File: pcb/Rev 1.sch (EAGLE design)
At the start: 50 parts, among them J1 3220-10-0100-00, U1 ATSAMD21G18A-MU, U2 AP3441, U3 TPS61089

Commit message: Worked on the schematic some more
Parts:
- added C26, C27, C28, C29, C30, C31, C32, C33, C42, C43, C44, C45, C46, C47, C48, C49, C50, C51, C58, C59: 1uF, Micromouse 2020:CAPACITOR0805
- added C34, C35, C36, C37, C38, C39, C40, C41, C52, C55: 0.1uF, Micromouse 2020:CAPACITOR0805
- added C53: 0.12uF, Micromouse 2020:CAPACITOR0805
- added C54: 6800pF, Micromouse 2020:CAPACITOR0805
- added C56, C57: 22pF, Micromouse 2020:CAPACITOR0805
- added D1, D10, D11, D2, D3, D4, D5, D6, D7, D8, D9: LED, Micromouse 2020:LED
- added D12, D13, D14, D15, D16, D17, D18, D19: SFH4545, Micromouse 2020:SFH4545
- added Q1, Q10, Q11, Q12, Q13, Q14, Q15, Q2, Q20, Q21, Q22, Q23, Q3, Q4, Q5, Q6, Q7, Q8, Q9: MMBT3904,215MMBT3904,215, Micromouse 2020:MMBT3904,215MMBT3904,215
- added Q16, Q17, Q18, Q19, Q24, Q25, Q26, Q27: TEFT4300, Micromouse 2020:TEFT4300
- added R15, R16, R17, R18, R19, R20, R21, R22, R23, R24, R25: (no value), Micromouse 2020:RESISTOR0805
- added R26, R27, R28, R29, R34, R35, R36, R37: 20R, Micromouse 2020:RESISTOR0805
- added R30, R31, R32, R33, R38, R39, R40, R41: 1k, Micromouse 2020:RESISTOR0805
- added R42, R43, R44, R45, R46, R47, R48, R49: 10k, Micromouse 2020:RESISTOR0805
- added R50, R51: 4.7k, Micromouse 2020:RESISTOR0805
- added U4: BNO055, Micromouse 2020:BNO055
- added U5: MCP73811, Micromouse 2020:MCP73811
- added XTAL3: 32.768kHz, Micromouse 2020:FC-135
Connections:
- new net IMU_INT: U4.INT
- new net IR1: Q12.B
- new net IR2: Q13.B
- new net IR3: Q14.B
- new net IR4: Q15.B
- new net IR5: Q20.B
- new net IR6: Q21.B
- new net IR7: Q22.B
- new net IR8: Q23.B
- new net LED0: Q2.B
- new net LED1: Q3.B
- new net LED2: Q4.B
- new net LED3: Q5.B
- new net LED4: Q6.B
- new net LED5: Q7.B
- new net LED6: Q8.B
- new net LED7: Q9.B
- new net LED8: Q10.B
- new net LED9: Q11.B
- new net N$16: Q1.B, U2.PG
- new net N$18: D1.OUT, Q1.C
- new net N$19: D1.IN, R15.P$1
- new net N$20: D2.OUT, Q2.C
- new net N$21: D2.IN, R16.P$1
- new net N$22: D3.OUT, Q3.C
- new net N$23: D3.IN, R17.P$1
- new net N$24: D4.OUT, Q4.C
- new net N$25: D4.IN, R18.P$1
- new net N$26: D5.OUT, Q5.C
- new net N$27: D5.IN, R19.P$1
- new net N$28: D6.OUT, Q6.C
- new net N$29: D6.IN, R20.P$1
- new net N$30: D7.OUT, Q7.C
- new net N$31: D7.IN, R21.P$1
- new net N$32: D8.OUT, Q8.C
- new net N$33: D8.IN, R22.P$1
- new net N$34: D9.OUT, Q9.C
- new net N$35: D9.IN, R23.P$1
- new net N$36: D10.OUT, Q10.C
- new net N$37: D10.IN, R24.P$1
- new net N$38: D11.OUT, Q11.C
- new net N$39: D11.IN, R25.P$1
- new net N$40: D12.OUT, Q12.C
- new net N$41: D12.IN, R26.P$2
- new net N$42: D13.OUT, Q13.C
- new net N$43: D13.IN, R27.P$2
- new net N$44: D14.OUT, Q14.C
- new net N$45: D14.IN, R28.P$2
- new net N$46: D15.OUT, Q15.C
- new net N$47: D15.IN, R29.P$2
- new net N$48: D16.OUT, Q20.C
- new net N$49: D16.IN, R34.P$2
- new net N$50: D17.OUT, Q21.C
- new net N$51: D17.IN, R35.P$2
- new net N$52: D18.OUT, Q22.C
- new net N$53: D18.IN, R36.P$2
- new net N$54: D19.OUT, Q23.C
- new net N$55: D19.IN, R37.P$2
- new net N$56: C55.P$2, U4.CAP
- new net N$57: R44.P$1, U4.!BOOTLOAD_PIN
- new net N$58: C56.P$2, U4.XOUT32, XTAL3.P$1
- new net N$59: R42.P$2, U4.PS1
- new net N$60: C57.P$2, U4.XIN32, XTAL3.P$2
- new net N$61: R45.P$2, U4.PS0
- new net N$62: R43.P$1, U4.!RESET
- new net N$63: R46.P$2, U4.COM3
- new net N$64: R47.P$2, U4.COM2
- new net N$66: R48.P$1, U5.CE
- new net N$67: R49.P$1, U5.PROG
- new net N$68: C59.P$2, U5.VBAT
- new net N$69: C58.P$2, R48.P$2, R49.P$2, U5.VDD
- new net PHOTO1: Q16.E, R30.P$2
- new net PHOTO2: Q17.E, R31.P$2
- new net PHOTO3: Q18.E, R32.P$2
- new net PHOTO4: Q19.E, R33.P$2
- new net PHOTO5: Q24.E, R38.P$2
- new net PHOTO6: Q25.E, R39.P$2
- new net PHOTO7: Q26.E, R40.P$2
- new net PHOTO8: Q27.E, R41.P$2
- new net SCL: R50.P$1, U4.COM1
- new net SDA: R51.P$1, U4.COM0
- net +3V3: now also C26.P$2, C27.P$2, C28.P$2, C29.P$2, C30.P$2, C31.P$2, C32.P$2, C33.P$2, C34.P$2, C35.P$2, C36.P$2, C37.P$2, C38.P$2, C39.P$2, C40.P$2, C41.P$2, C42.P$2, C43.P$2, C44.P$2, C45.P$2, C46.P$2, C47.P$2, C48.P$2, C49.P$2, C50.P$2, C51.P$2, C52.P$2, C53.P$2, C54.P$2, Q16.C, Q17.C, Q18.C, Q19.C, Q24.C, Q25.C, Q26.C, Q27.C, R15.P$2, R16.P$2, R17.P$2, R18.P$2, R19.P$2, R20.P$2, R21.P$2, R22.P$2, R23.P$2, R24.P$2, R25.P$2, R26.P$1, R27.P$1, R28.P$1, R29.P$1, R34.P$1, R35.P$1, R36.P$1, R37.P$1, R43.P$2, R44.P$2, R50.P$2, R51.P$2, U4.VDD, U4.VDDIO
- net GND: now also C26.P$1, C27.P$1, C28.P$1, C29.P$1, C30.P$1, C31.P$1, C32.P$1, C33.P$1, C34.P$1, C35.P$1, C36.P$1, C37.P$1, C38.P$1, C39.P$1, C40.P$1, C41.P$1, C42.P$1, C43.P$1, C44.P$1, C45.P$1, C46.P$1, C47.P$1, C48.P$1, C49.P$1, C50.P$1, C51.P$1, C52.P$1, C53.P$1, C54.P$1, C55.P$1, C56.P$1, C57.P$1, C58.P$1, C59.P$1, Q1.E, Q10.E, Q11.E, Q12.E, Q13.E, Q14.E, Q15.E, Q2.E, Q20.E, Q21.E, Q22.E, Q23.E, Q3.E, Q4.E, Q5.E, Q6.E, Q7.E, Q8.E, Q9.E, R30.P$1, R31.P$1, R32.P$1, R33.P$1, R38.P$1, R39.P$1, R40.P$1, R41.P$1, R42.P$1, R45.P$1, R46.P$1, R47.P$1, U4.GND, U4.GNDIO, U5.VSS
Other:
- note added: "TODO: Battery"
- note added: "TODO: Disconnecting circuit"
- note added: "TODO: USB port"
- note removed: "TODO: Power LED"

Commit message: Did a lot of the schematic
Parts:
- removed L1: (no value), Micromouse 2020:INDUCTOR
- added A1, A2, A3, A4: ENCODER, Micromouse 2020:ENCODER
- added A5: HC-05, Micromouse 2020:HC-05
- added C60, C67, C70, C73, C76, C78: 1uF, Micromouse 2020:CAPACITOR0805
- added C61: 10uF, Micromouse 2020:CAPACITOR0805
- added C62: 100uF, Micromouse 2020:EEE-1EA101AP
- added C63: 300pF, Micromouse 2020:CAPACITOR0805
- added C64: 2.2uF, Micromouse 2020:CAPACITOR0805
- added C65, C68, C71, C74, C77: 0.1uF, Micromouse 2020:CAPACITOR0805
- added C66, C69, C72, C75: 22uF, Micromouse 2020:865080542006
- added FB1: (no value), Micromouse 2020:FERRITE
- added J2: 10118194-0001LF, Micromouse 2020:10118194-0001LF
- added J3: B2B-PH-K-S(LF)(SN), Micromouse 2020:B2B-PH-K-S(LF)(SN)
- added Q28, Q29, Q32: SI7157DP, Micromouse 2020:SI7157DP
- added Q30, Q31, Q33, Q34: MMBT3906, Micromouse 2020:MMBT3906
- added R52, R56, R59, R63, R67, R68, R70, R71, R72, R73, R74, R75, R76: 10k, Micromouse 2020:RESISTOR0805
- added R53, R54, R57, R58: 100k, Micromouse 2020:RESISTOR0805
- added R55, R60: 68k, Micromouse 2020:RESISTOR0805
- added R61, R62: 0R, Micromouse 2020:RESISTOR0805
- added R64, R65, R66: 30k, Micromouse 2020:RESISTOR0805
- added R69: 10k\, Micromouse 2020:RESISTOR0805
- added R77, R78, R79, R80, R81, R82, R83, R84, R85, R86: 470k, Micromouse 2020:RESISTOR0805
- added SW1: 210-10MS, Micromouse 2020:210-10MS
- added TP1, TP2, TP3, TP4, TP5, TP6, TP7, TP8, TP9: TESTPOINT, Micromouse 2020:TESTPOINT
- added U10, U7, U8, U9: DRV8871, Micromouse 2020:DRV8871
- added U6: (no value), Micromouse 2020:MCP1501
- D1, D10, D11, D2, D3, D4, D5, D6, D7, D8, D9: value LED -> LED1206; device Micromouse 2020:LED -> Micromouse 2020:LED1206
- R4: value 0R -> 30k
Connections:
- new net +5V: C58.P$2, C60.P$2, J2.VCC, Q28.G, Q32.S, Q34.E, R48.P$2, R49.P$2, R61.P$1, TP5.P$1, U5.VDD
- new net BT_EN: A5.EN
- new net BT_RX: A5.TXD
- new net BT_STATE: A5.STATE
- new net BT_TX: A5.RXD
- new net ENCODER_1A: A1.OUTA
- new net ENCODER_1B: A1.OUTB
- new net ENCODER_2A: A2.OUTA
- new net ENCODER_2B: A2.OUTB
- new net ENCODER_3A: A3.OUTA
- new net ENCODER_3B: A3.OUTB
- new net ENCODER_4A: A4.OUTA
- new net ENCODER_4B: A4.OUTB
- new net MOTOR_1A: U7.IN1
- new net MOTOR_1B: U7.IN2
- new net MOTOR_2A: U8.IN1
- new net MOTOR_2B: U8.IN2
- new net MOTOR_3A: U9.IN1
- new net MOTOR_3B: U9.IN2
- new net MOTOR_4A: U10.IN1
- new net MOTOR_4B: U10.IN2
- new net N$100: R73.P$2, SW1.4B
- new net N$101: R74.P$2, SW1.3B
- new net N$102: R75.P$2, SW1.2B
- new net N$103: R76.P$2, SW1.1B
- new net N$65: C59.P$2, C61.P$2, J3.1, Q28.S, R62.P$1, TP3.P$1, U5.VBAT
- new net N$70: Q31.B, R56.P$1
- new net N$71: Q30.B, R56.P$2
- new net N$72: J2.ID, R52.P$2
- new net N$73: J2.D+, R53.P$2
- new net N$74: J2.D-, R54.P$2
- new net N$75: Q29.G, Q31.C, R57.P$1
- new net N$76: Q32.G, Q33.C, R58.P$2
- new net N$77: Q34.B, R59.P$1
- new net N$78: Q33.B, R59.P$2
- new net N$79: Q34.C, R60.P$2
- new net N$80: A1.MA, U7.OUT1
- new net N$82: R63.P$1, U6.!SHDN
- new net N$83: R4.P$2, U7.ILIM
- new net N$84: A1.MB, U7.OUT2
- new net N$85: R64.P$2, U8.ILIM
- new net N$86: A2.MA, U8.OUT1
- new net N$87: A2.MB, U8.OUT2
- new net N$88: R65.P$2, U9.ILIM
- new net N$89: A3.MA, U9.OUT1
- new net N$90: A3.MB, U9.OUT2
- new net N$91: R66.P$2, U10.ILIM
- new net N$92: A4.MA, U10.OUT1
- new net N$93: A4.MB, U10.OUT2
- new net N$94: R67.P$2, SW1.10B
- new net N$95: R68.P$2, SW1.9B
- new net N$96: R69.P$2, SW1.8B
- new net N$97: R70.P$2, SW1.7B
- new net N$98: R71.P$2, SW1.6B
- new net N$99: R72.P$2, SW1.5B
- new net SW0: R86.P$1, SW1.1A
- new net SW1: R85.P$1, SW1.2A
- new net SW2: R84.P$1, SW1.3A
- new net SW3: R83.P$1, SW1.4A
- new net SW4: R82.P$1, SW1.5A
- new net SW5: R81.P$1, SW1.6A
- new net SW6: R80.P$1, SW1.7A
- new net SW7: R79.P$1, SW1.8A
- new net SW8: R78.P$1, SW1.9A
- new net SW9: R77.P$1, SW1.10A
- net +12V: now also C65.P$2, C66.+, C68.P$2, C69.+, C71.P$2, C72.+, C74.P$2, C75.+, TP7.P$1, U10.VM, U7.VM, U8.VM, U9.VM
- net +3V3: now also A1.VCC, A2.VCC, A3.VCC, A4.VCC, A5.VCC, C64.P$2, C67.P$2, C70.P$2, C73.P$2, C76.P$2, C77.P$2, C78.P$2, FB1.P$2, R63.P$2, R77.P$2, R78.P$2, R79.P$2, R80.P$2, R81.P$2, R82.P$2, R83.P$2, R84.P$2, R85.P$2, R86.P$2, TP6.P$1, U6.VDD; no longer L1.P$2, R4.P$2
- net +3V7: now also C62.+, Q29.D, Q31.E, Q32.D, Q33.E, R61.P$2, R62.P$2, TP4.P$1
- net GND: now also A1.GND, A2.GND, A3.GND, A4.GND, A5.GND, C60.P$1, C61.P$1, C62.-, C63.P$1, C64.P$1, C65.P$1, C66.-, C67.P$1, C68.P$1, C69.-, C70.P$1, C71.P$1, C72.-, C73.P$1, C74.P$1, C75.-, C76.P$1, C77.P$1, C78.P$1, J2.GND, J3.2, R4.P$1, R52.P$1, R53.P$1, R54.P$1, R58.P$1, R60.P$1, R64.P$1, R65.P$1, R66.P$1, R67.P$1, R68.P$1, R69.P$1, R70.P$1, R71.P$1, R72.P$1, R73.P$1, R74.P$1, R75.P$1, R76.P$1, U10.GND, U10.PGND, U6.GND, U7.GND, U7.PGND, U8.GND, U8.PGND, U9.GND, U9.PGND
- net IR1: now also TP8.P$1
- net N$4: now also FB1.P$1; no longer L1.P$1
- net N$68: now also Q30.C, R55.P$1; no longer C59.P$2, U5.VBAT
- net N$69: now also Q28.D, Q29.S, Q30.E, R55.P$2, R57.P$2; no longer C58.P$2, R48.P$2, R49.P$2, U5.VDD
- net PHOTO1: now also TP9.P$1
- net SCL: now also TP2.P$1
- net SDA: now also TP1.P$1
- net VREFA: now also C63.P$2, U6.OUT; no longer R4.P$1
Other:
- note added: "Do not populate"
- note removed: "TODO: Add real voltage reference"
- note removed: "TODO: Battery"
- note removed: "TODO: Disconnecting circuit"
- note removed: "TODO: Switch inductor to Ferite bead"
- note removed: "TODO: USB port"

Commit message: Added encoder schematic
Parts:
- A1, A2, A3, A4: value ENCODER -> ENCODERSLOT; device Micromouse 2020:ENCODER -> Micromouse 2020:ENCODERSLOT
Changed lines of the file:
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@@
 <part name="P+56" library="Micromouse 2020" deviceset="+12V" device=""/>
 <part name="C62" library="Micromouse 2020" deviceset="EEE-1EA101AP" device="" package3d_urn="urn:adsk.eagle:package:15328765/1" value="100uF"/>
-<part name="A1" library="Micromouse 2020" deviceset="ENCODER" device=""/>
+<part name="A1" library="Micromouse 2020" deviceset="ENCODER" device="SLOT" value="ENCODERSLOT"/>
 <part name="GND72" library="Micromouse 2020" deviceset="GND" device=""/>
 <part name="P+57" library="Micromouse 2020" deviceset="+3V3" device=""/>
@@
 <part name="C69" library="Micromouse 2020" deviceset="865080542006" device="" package3d_urn="urn:adsk.eagle:package:15317400/1" value="22uF"/>
 <part name="P+59" library="Micromouse 2020" deviceset="+12V" device=""/>
-<part name="A2" library="Micromouse 2020" deviceset="ENCODER" device=""/>
+<part name="A2" library="Micromouse 2020" deviceset="ENCODER" device="SLOT" value="ENCODERSLOT"/>
 <part name="GND77" library="Micromouse 2020" deviceset="GND" device=""/>
 <part name="P+60" library="Micromouse 2020" deviceset="+3V3" device=""/>
@@
 <part name="C72" library="Micromouse 2020" deviceset="865080542006" device="" package3d_urn="urn:adsk.eagle:package:15317400/1" value="22uF"/>
 <part name="P+62" library="Micromouse 2020" deviceset="+12V" device=""/>
-<part name="A3" library="Micromouse 2020" deviceset="ENCODER" device=""/>
+<part name="A3" library="Micromouse 2020" deviceset="ENCODER" device="SLOT" value="ENCODERSLOT"/>
 <part name="GND82" library="Micromouse 2020" deviceset="GND" device=""/>
 <part name="P+63" library="Micromouse 2020" deviceset="+3V3" device=""/>
@@
 <part name="C75" library="Micromouse 2020" deviceset="865080542006" device="" package3d_urn="urn:adsk.eagle:package:15317400/1" value="22uF"/>
 <part name="P+65" library="Micromouse 2020" deviceset="+12V" device=""/>
-<part name="A4" library="Micromouse 2020" deviceset="ENCODER" device=""/>
+<part name="A4" library="Micromouse 2020" deviceset="ENCODER" device="SLOT" value="ENCODERSLOT"/>
 <part name="GND87" library="Micromouse 2020" deviceset="GND" device=""/>
 <part name="P+66" library="Micromouse 2020" deviceset="+3V3" device=""/>

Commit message: Updated the schematic
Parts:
- removed L3: (no value), Micromouse 2020:INDUCTOR
- removed R3: 0R, Micromouse 2020:RESISTOR0805
- added C79: 0.1uF, Micromouse 2020:CAPACITOR0805
- added C80: 100uF, Micromouse 2020:EEE-1EA101AP
- added FB2, FB3: (no value), Micromouse 2020:FERRITE
- added L1: 10uH, Micromouse 2020:104CDMCC
- C11, C12: value 15pF -> 22pF
- C13: value 15pF -> 6.8pF
- C14: value 15pF -> 10pF
- C16, C18, C19: device Micromouse 2020:CAPACITOR0805 -> Micromouse 2020:865080542006
- C20: value (none) -> 0.1uF
- C21: value (none) -> 2.2uF
- C22, C25: value (none) -> 22uF; device Micromouse 2020:CAPACITOR0805 -> Micromouse 2020:865080542006
- C23: value (none) -> 33pF
- C24: value (none) -> 680pF
- L2: value 2.2uH -> 3.3uH; device Micromouse 2020:INDUCTOR -> Micromouse 2020:NRS5040
- R11: value (none) -> 150k
- R12: value (none) -> 348k
- R13: value (none) -> 18k
- R14: value (none) -> 160k
- R16, R17, R18, R19, R20, R21, R22, R23, R24, R25: value (none) -> 30R
- R26, R27, R28, R29, R34, R35, R36, R37: value 20R -> 17R
- R9: value (none) -> 270k
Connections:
- new net N$104: C61.P$2, J3.1, R61.P$2, R62.P$2
- net +12V: now also C25.+, C80.+; no longer C25.P$2
- net +3V3: now also C18.+, C19.+; no longer C18.P$2, C19.P$2
- net +3V7: now also C16.+, C22.+, L1.P$2, R61.P$1; no longer C16.P$2, C22.P$2, L3.P$2, R61.P$2, R62.P$2
- net +5V: no longer R61.P$1
- net GND: now also C16.-, C18.-, C19.-, C22.-, C25.-, C79.P$1, C80.-; no longer C16.P$1, C18.P$1, C19.P$1, C22.P$1, C25.P$1
- net N$10: now also L1.P$1; no longer L3.P$1
- net N$65: no longer C61.P$2, J3.1
- net VREFA: now also C79.P$2, FB2.P$1, FB2.P$2, FB3.P$1; no longer R3.P$2
- net VREFB: now also FB3.P$2; no longer R3.P$1
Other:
- note removed: "TODO: Calculate values"
- moved on the sheet: C10, C61, J3, R61, R62

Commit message: Started to lay out board
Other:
- note removed: "TODO: Calculate capacitor values"
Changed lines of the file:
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@@
 <description>IMU</description>
 <plain>
-<text x="-55.88" y="-45.72" size="1.778" layer="91">TODO: Calculate capacitor values</text>
 </plain>
 <instances>

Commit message: Sorted into groups
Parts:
- R15: value (none) -> 30R
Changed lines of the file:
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@@
 <part name="Q1" library="Micromouse 2020" deviceset="MMBT3904,215" device="MMBT3904,215" package3d_urn="urn:adsk.eagle:package:12395711/1"/>
 <part name="D1" library="Micromouse 2020" deviceset="LED" device="1206"/>
-<part name="R15" library="Micromouse 2020" deviceset="RESISTOR" device="0805"/>
+<part name="R15" library="Micromouse 2020" deviceset="RESISTOR" device="0805" value="30R"/>
 <part name="P+12" library="Micromouse 2020" deviceset="+3V3" device=""/>
 <part name="GND22" library="Micromouse 2020" deviceset="GND" device=""/>

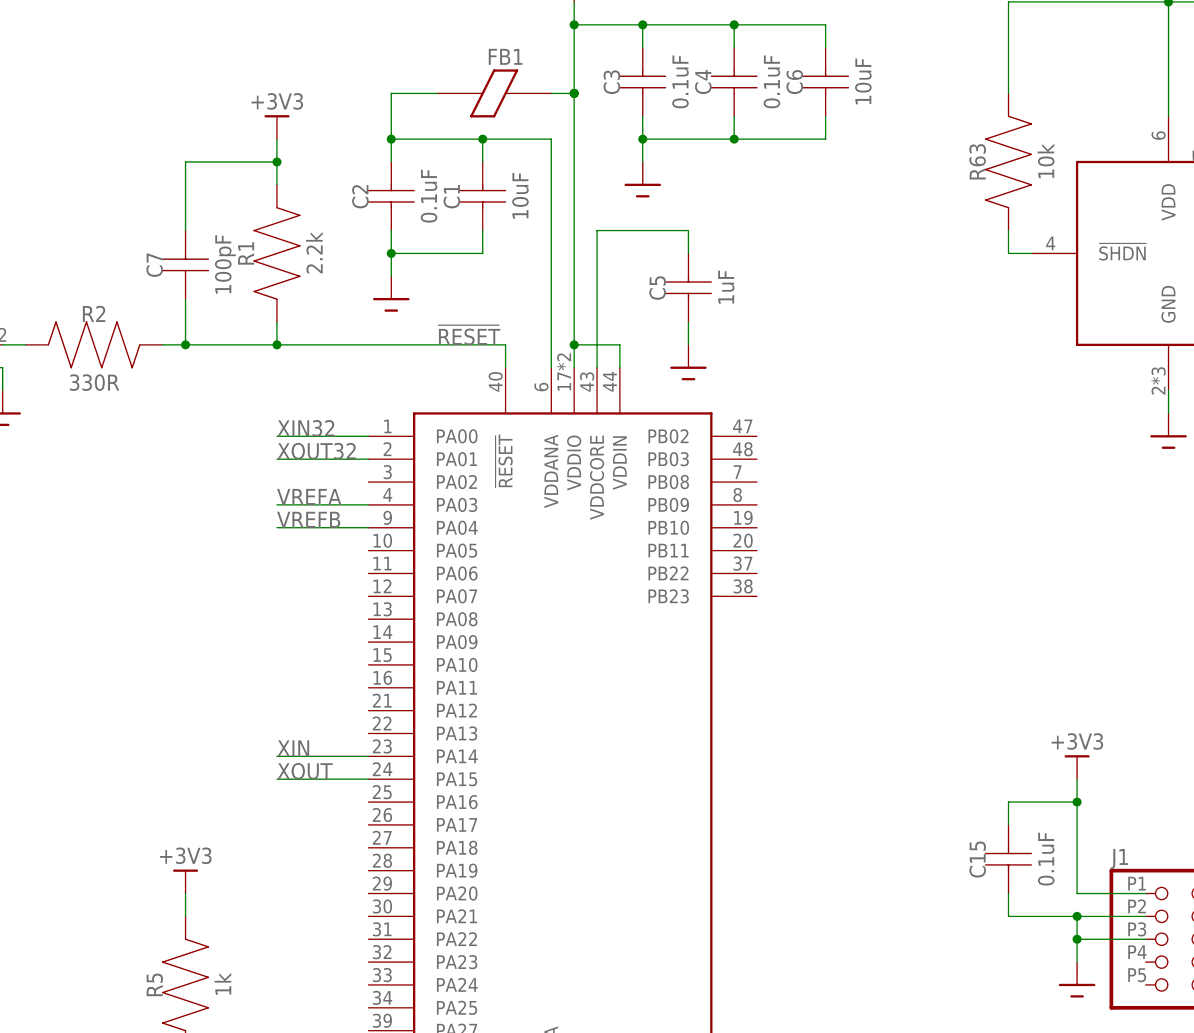
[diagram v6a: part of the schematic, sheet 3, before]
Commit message: Placed the majority of the components
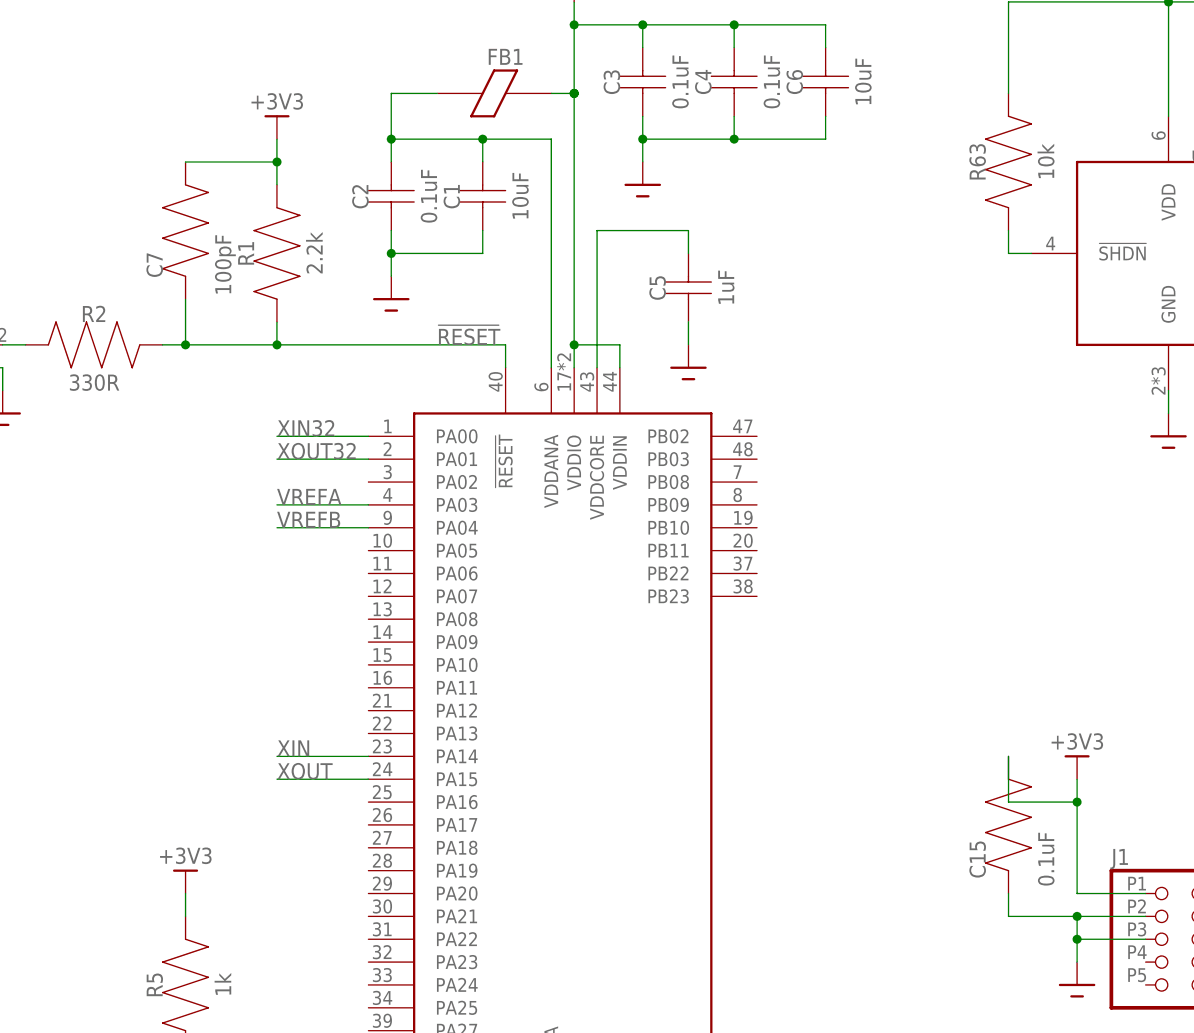
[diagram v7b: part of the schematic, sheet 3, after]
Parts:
- C1, C10, C11, C12, C13, C14, C2, C20, C21, C23, C24, C3, C4, C5, C6, C63, C64, C79, C8, C9: device Micromouse 2020:CAPACITOR0805 -> Micromouse 2020:CAPACITOR0402
- C15, C7: device Micromouse 2020:CAPACITOR0805 -> Micromouse 2020:RESISTOR0603
- C33, C40, C52, C53, C54, C55, C56, C57, C77: device Micromouse 2020:CAPACITOR0805 -> Micromouse 2020:CAPACITOR0603
- FB1, FB2, FB3: device Micromouse 2020:FERRITE -> Micromouse 2020:FERRITE0402
- R1, R10, R11, R2, R42, R43, R44, R45, R46, R47, R5, R50, R51, R55, R56, R57, R67, R68, R69, R70, R71, R72, R73, R74, R75, R76, R77, R78, R79, R80, R81, R82, R83, R84, R85, R86: device Micromouse 2020:RESISTOR0805 -> Micromouse 2020:RESISTOR0603
- R12, R13, R14, R48, R49, R52, R53, R54, R63, R9: device Micromouse 2020:RESISTOR0805 -> Micromouse 2020:RESISTOR0402
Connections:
- new net N$999: C63.P$2, C8.P$2, C9.P$2, FB2.P$1, FB3.P$1, U6.OUT
- net VREFA: no longer C63.P$2, C8.P$2, C9.P$2, FB2.P$1, FB3.P$1, U6.OUT
